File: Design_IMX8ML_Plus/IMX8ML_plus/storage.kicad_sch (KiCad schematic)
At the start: 3 parts, among them U1 MIMX8ML8CVNKZAB, U3 SDINBDG4-8G, U5 MT25QUxxxxxx1xW7

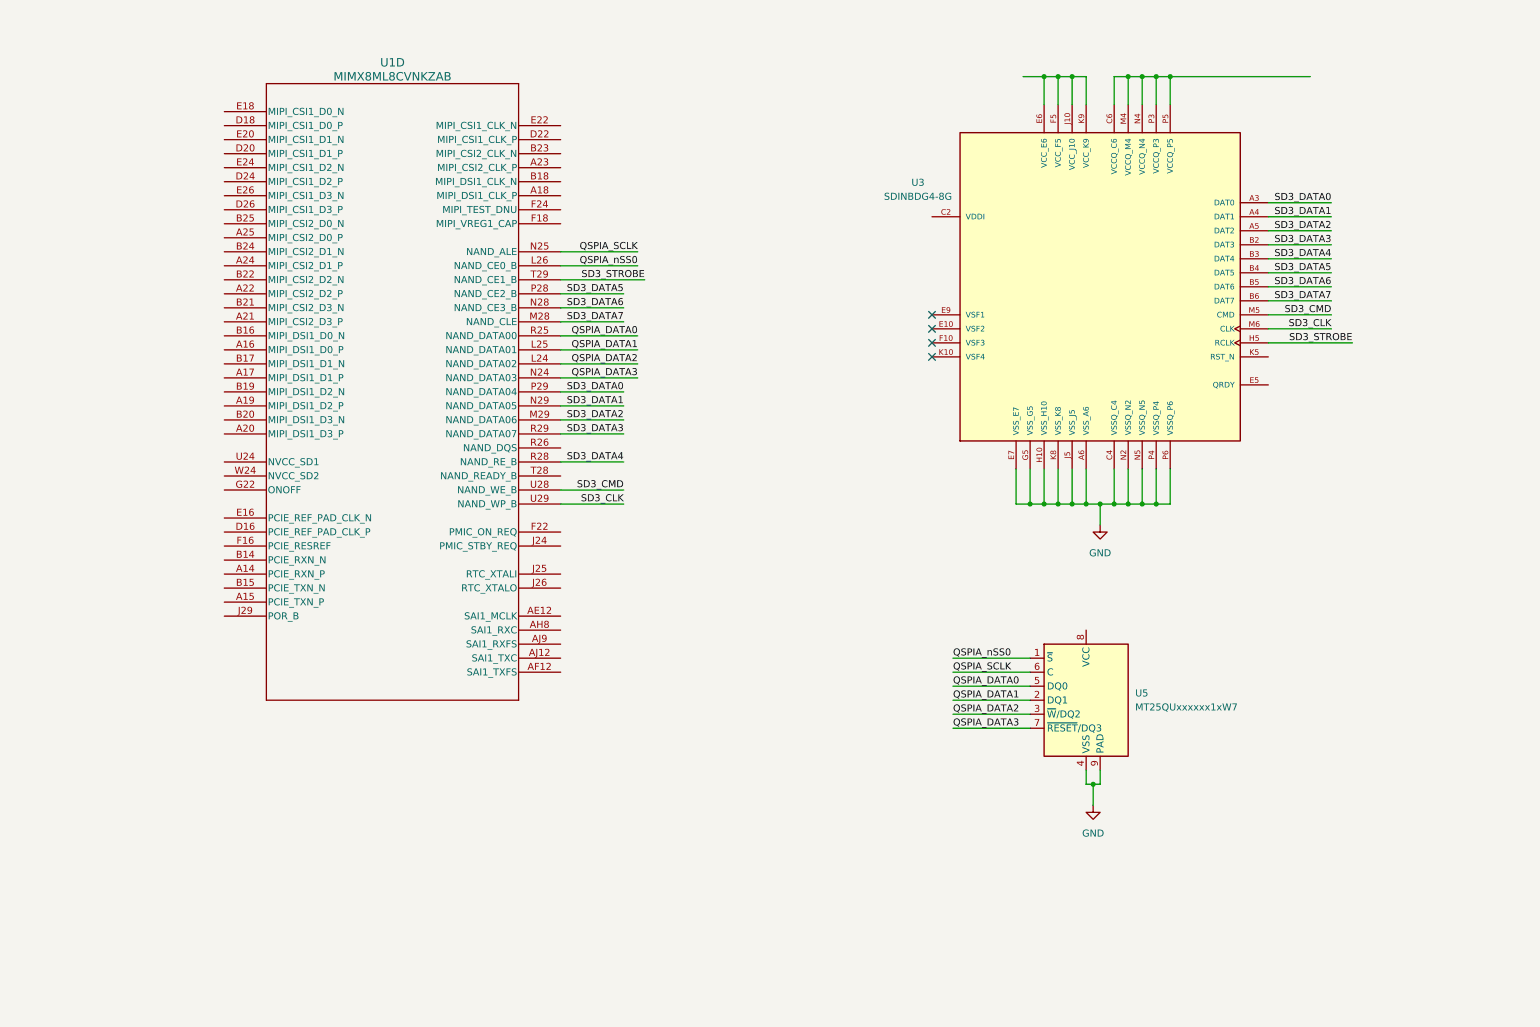
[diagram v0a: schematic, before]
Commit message: Add interface io pins
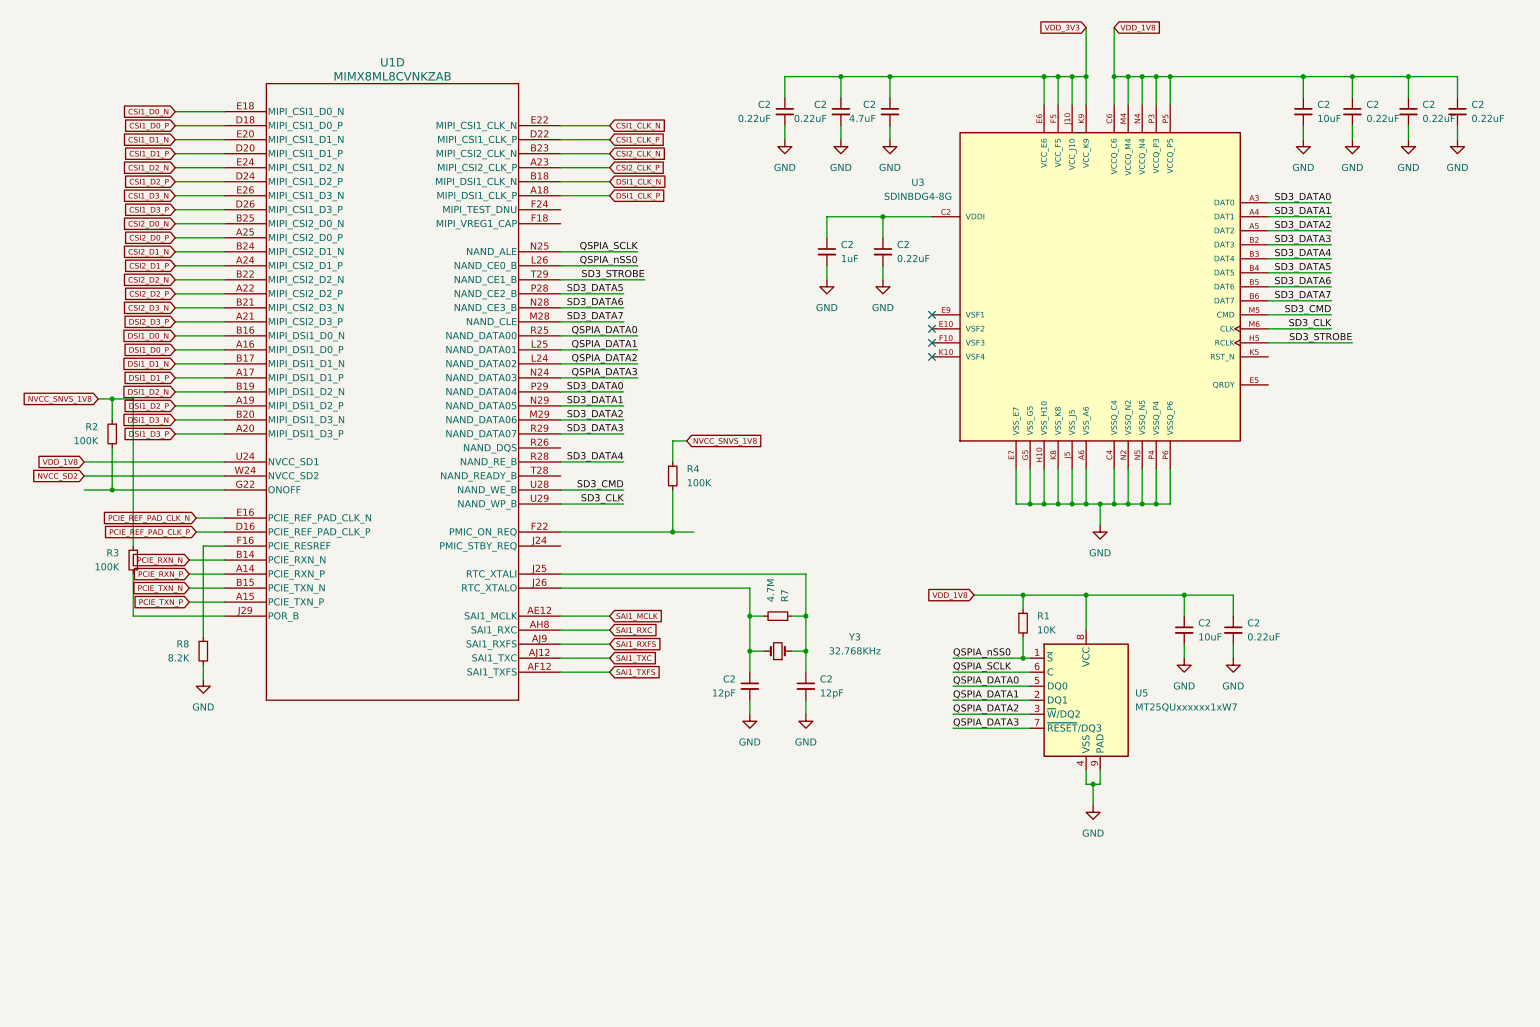
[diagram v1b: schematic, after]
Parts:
- added C2 (x7): 0.22uF, Capacitor_SMD:C_0201_0603Metric_Pad0.64x0.40mm_HandSolder, symbol Device:C_Small
- added C2: 4.7uF, Capacitor_SMD:C_0402_1005Metric_Pad0.74x0.62mm_HandSolder, symbol Device:C_Small
- added C2: 1uF, Capacitor_SMD:C_0201_0603Metric_Pad0.64x0.40mm_HandSolder, symbol Device:C_Small
- added C2 (x2): 12pF, Capacitor_SMD:C_0201_0603Metric_Pad0.64x0.40mm_HandSolder, symbol Device:C_Small
- added C2 (x2): 10uF, Capacitor_SMD:C_0402_1005Metric_Pad0.74x0.62mm_HandSolder, symbol Device:C_Small
- added R1: 10K, Resistor_SMD:R_0402_1005Metric_Pad0.72x0.64mm_HandSolder, symbol Device:R_Small
- added R2, R3, R4: 100K, Resistor_SMD:R_0402_1005Metric_Pad0.72x0.64mm_HandSolder, symbol Device:R_Small
- added R7: 4.7M, Resistor_SMD:R_0402_1005Metric_Pad0.72x0.64mm_HandSolder, symbol Device:R_Small
- added R8: 8.2K, Resistor_SMD:R_0402_1005Metric_Pad0.72x0.64mm_HandSolder, symbol Device:R_Small
- added Y3: 32.768KHz, Capacitor_SMD:C_0504_1310Metric, symbol Device:Crystal_Small
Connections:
- net GND: now also C2.2, C2.2, C2.2, C2.2, C2.2, C2.2, C2.2, C2.2, C2.2, C2.2, C2.2, C2.2, C2.2, R8.2
- net QSPIA_nSS0: now also R1.2
- net VDD_1V8: now reaches U5.8 (VCC)
- net VDD_1V8: now also U1.U24 (NVCC_SD1), U3.C6 (VCCQ_C6), U3.M4 (VCCQ_M4), U3.N4 (VCCQ_N4), U3.P3 (VCCQ_P3), U3.P5 (VCCQ_P5), C2.1, C2.1, C2.1, C2.1, C2.1, C2.1, R1.1
- net PCIE_RXN_P: now reaches U1.A14 (PCIE_RXN_P)
- net PCIE_TXN_P: now reaches U1.A15 (PCIE_TXN_P)
- net DSI1_D0_P: now reaches U1.A16 (MIPI_DSI1_D0_P)
- net DSI1_D1_P: now reaches U1.A17 (MIPI_DSI1_D1_P)
- net DSI1_CLK_P: now reaches U1.A18 (MIPI_DSI1_CLK_P)
- net DSI1_D2_P: now reaches U1.A19 (MIPI_DSI1_D2_P)
- net DSI1_D3_P: now reaches U1.A20 (MIPI_DSI1_D3_P)
- net DSI2_D3_P: now reaches U1.A21 (MIPI_CSI2_D3_P)
- net CSI2_D2_P: now reaches U1.A22 (MIPI_CSI2_D2_P)
- net CSI2_CLK_P: now reaches U1.A23 (MIPI_CSI2_CLK_P)
- net CSI2_D1_P: now reaches U1.A24 (MIPI_CSI2_D1_P)
- net CSI2_D0_P: now reaches U1.A25 (MIPI_CSI2_D0_P)
- net SAI1_MCLK: now reaches U1.AE12 (SAI1_MCLK)
- net SAi1_TXFS: now reaches U1.AF12 (SAI1_TXFS)
- net SAI1_RXC: now reaches U1.AH8 (SAI1_RXC)
- net SAI1_TXC: now reaches U1.AJ12 (SAI1_TXC)
- net SAI1_RXFS: now reaches U1.AJ9 (SAI1_RXFS)
- net PCIE_RXN_N: now reaches U1.B14 (PCIE_RXN_N)
- net PCIE_TXN_N: now reaches U1.B15 (PCIE_TXN_N)
- net DSI1_D0_N: now reaches U1.B16 (MIPI_DSI1_D0_N)
- net DSI1_D1_N: now reaches U1.B17 (MIPI_DSI1_D1_N)
- net DSI1_CLK_N: now reaches U1.B18 (MIPI_DSI1_CLK_N)
- net DSI1_D2_N: now reaches U1.B19 (MIPI_DSI1_D2_N)
- net DSI1_D3_N: now reaches U1.B20 (MIPI_DSI1_D3_N)
- net CSI2_D3_N: now reaches U1.B21 (MIPI_CSI2_D3_N)
- net CSI2_D2_N: now reaches U1.B22 (MIPI_CSI2_D2_N)
- net CSI2_CLK_N: now reaches U1.B23 (MIPI_CSI2_CLK_N)
- net CSI2_D1_N: now reaches U1.B24 (MIPI_CSI2_D1_N)
- net CSI2_D0_N: now reaches U1.B25 (MIPI_CSI2_D0_N)
- net PCIE_REF_PAD_CLK_P: now reaches U1.D16 (PCIE_REF_PAD_CLK_P)
- net CSI1_D0_P: now reaches U1.D18 (MIPI_CSI1_D0_P)
- net CSI1_D1_P: now reaches U1.D20 (MIPI_CSI1_D1_P)
- net CSI1_CLK_P: now reaches U1.D22 (MIPI_CSI1_CLK_P)
- net CSI1_D2_P: now reaches U1.D24 (MIPI_CSI1_D2_P)
- net CSI1_D3_P: now reaches U1.D26 (MIPI_CSI1_D3_P)
- net PCIE_REF_PAD_CLK_N: now reaches U1.E16 (PCIE_REF_PAD_CLK_N)
- net CSI1_D0_N: now reaches U1.E18 (MIPI_CSI1_D0_N)
- net CSI1_D1_N: now reaches U1.E20 (MIPI_CSI1_D1_N)
- net CSI1_CLK_N: now reaches U1.E22 (MIPI_CSI1_CLK_N)
- net CSI1_D2_N: now reaches U1.E24 (MIPI_CSI1_D2_N)
- net CSI1_D3_N: now reaches U1.E26 (MIPI_CSI1_D3_N)
- net at U1.F16 (PCIE_RESREF): now also R8.1
- net at U1.F22 (PMIC_ON_REQ): now also R4.2
- net at U1.G22 (ONOFF): now also R2.2
- net at U1.J25 (RTC_XTALI): now also C2.1, R7.1, Y3.1
- net at U1.J26 (RTC_XTALO): now also C2.1, R7.2, Y3.2
- net at U1.J29 (POR_B): now also R3.2
- net NVCC_SD2: now reaches U1.W24 (NVCC_SD2)
- net at U3.C2 (VDDI): now also C2.1, C2.1
- net VDD_3V3: now reaches U3.E6 (VCC_E6), U3.F5 (VCC_F5), U3.J10 (VCC_J10), U3.K9 (VCC_K9)
- net VDD_3V3: now also C2.1, C2.1, C2.1
- new net NVCC_SNVS_1V8: R2.1, R3.1, R4.1

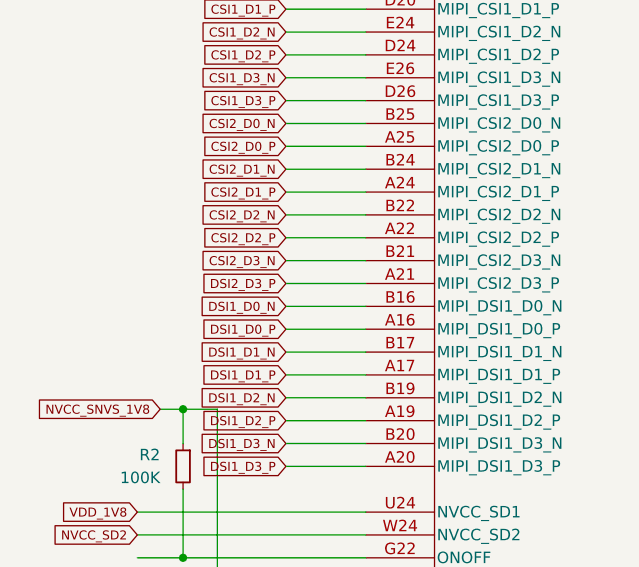
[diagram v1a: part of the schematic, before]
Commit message: Update schematic and add ethernet interface ksz9131rn
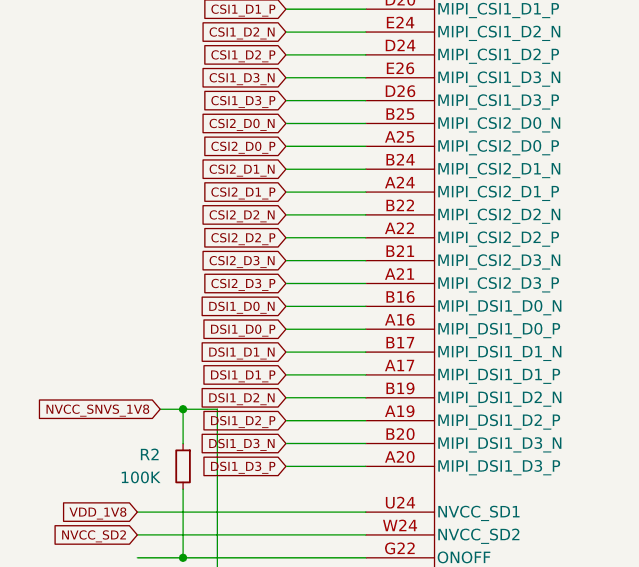
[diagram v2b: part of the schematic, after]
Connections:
- net DSI2_D3_P renamed CSI2_D3_P
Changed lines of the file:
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@@
     )
   )
-  (global_label "DSI2_D3_P" (shape input) (at 40.64 71.12 180) (fields_autoplaced)
+  (global_label "CSI2_D3_P" (shape input) (at 40.64 71.12 180) (fields_autoplaced)
     (effects (font (size 1 1)) (justify right))
     (property "Intersheetrefs" "${INTERSHEET_REFS}" (at 30.4949 71.12 0)

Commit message: Add SPB228 WIFI/BLE module
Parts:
- renumbered C2 to C144, C2 to C145, C2 to C85, C2 to C86, C2 to C87, C2 to C88, C2 to C89, C2 to C90, C2 to C91, C2 to C92, C2 to C93, C2 to C94, C2 to C95

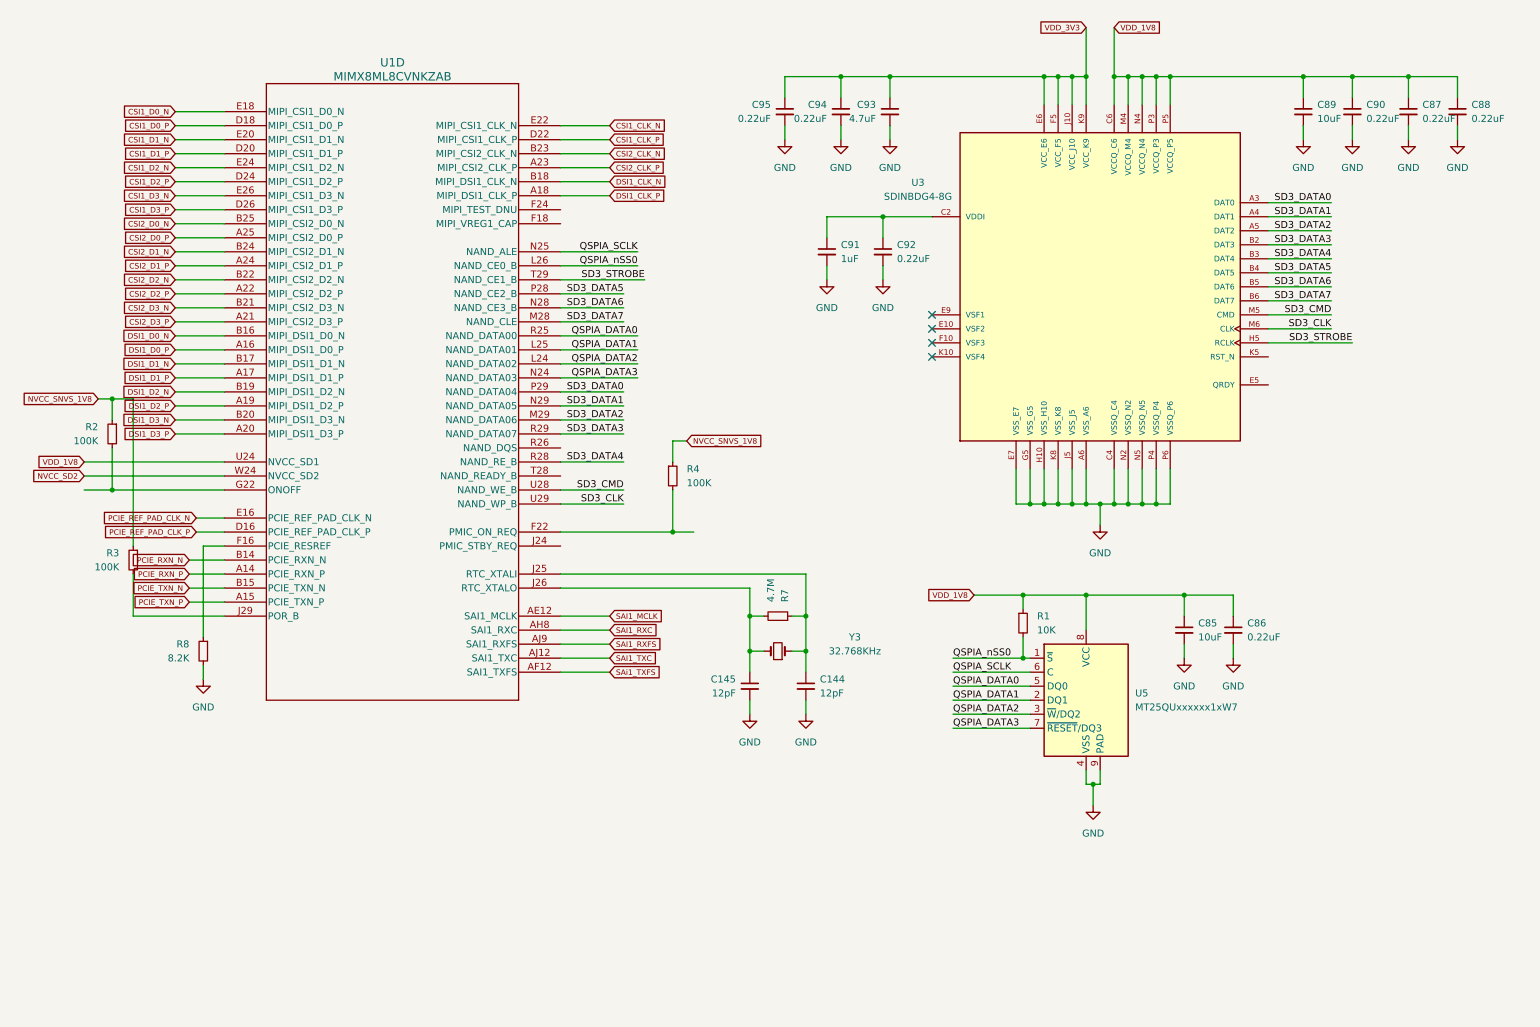
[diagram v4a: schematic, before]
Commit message: [IMX8ML-Processor] Reorganization of the pinout conector since processor to conectors
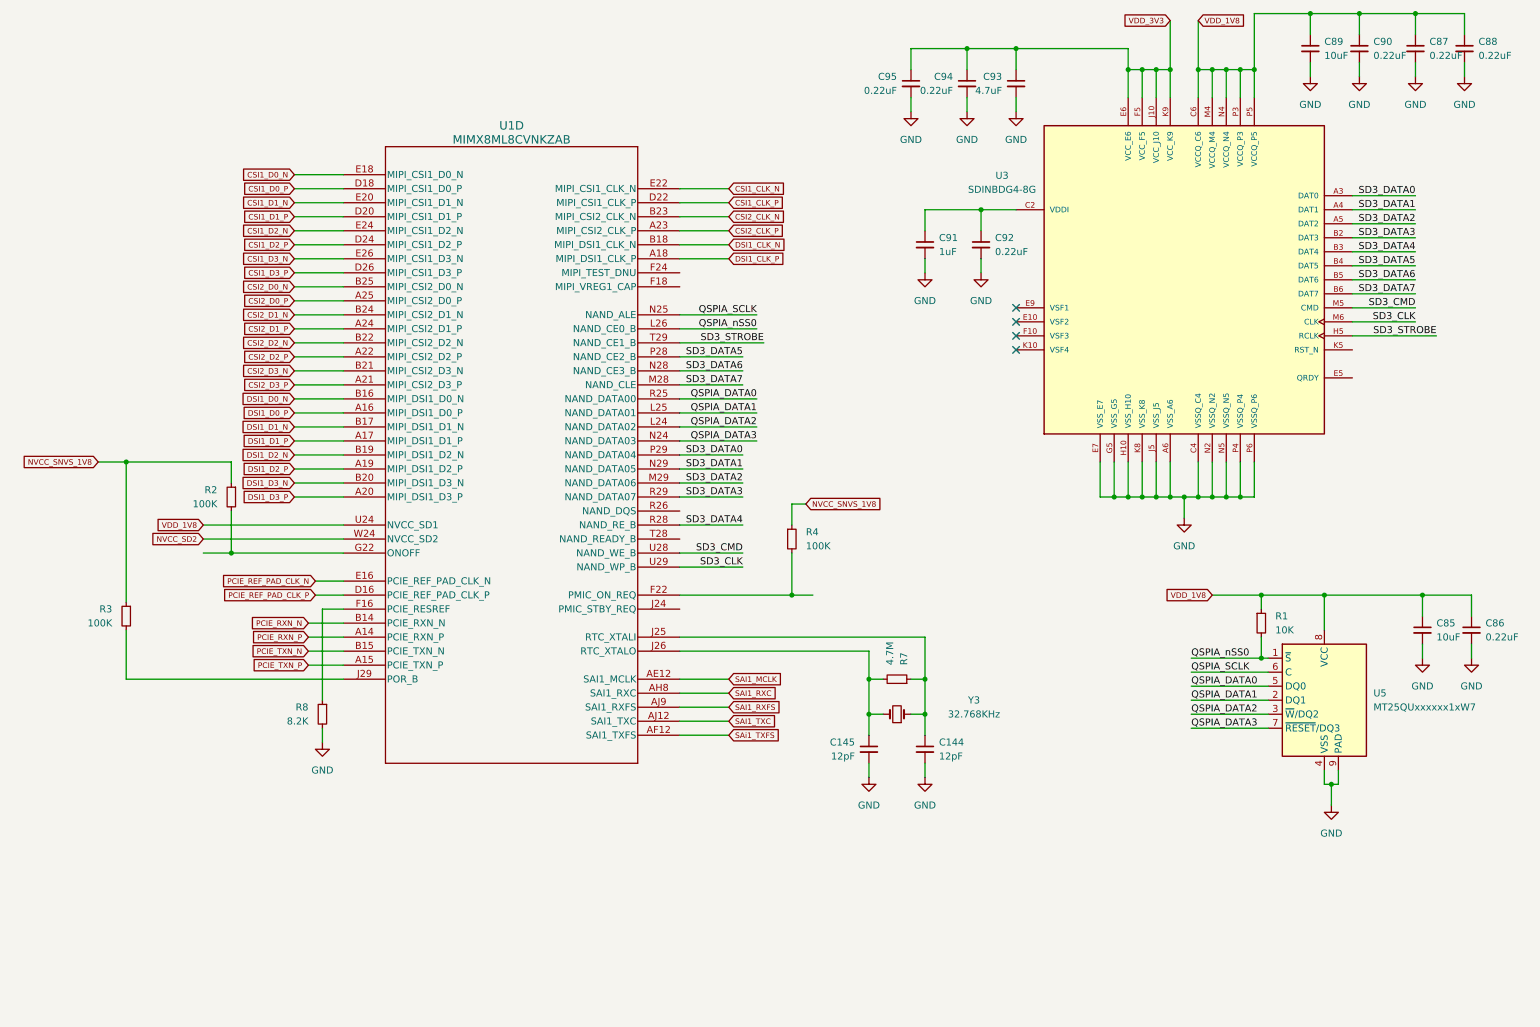
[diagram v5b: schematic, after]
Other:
- moved on the sheet: C144, C145, C85, C86, C87, C88, C89, C90, C91, C92, C93, C94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

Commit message: [PROCESSOR] Create zones It added power zones in the four layer
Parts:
- renumbered C145 to C115, C95 to C116, C91 to C117, C144 to C118, C94 to C119, C92 to C120, C93 to C121, C89 to C122, C90 to C123, C87 to C124, C85 to C125, C88 to C126, C86 to C127, R3 to R10, R2 to R11, R8 to R12, R4 to R13, R7 to R14, R1 to R15, U3 to U4, Y3 to Y2
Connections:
- net ON/OFF: now reaches R11.2, U1.G22 (ONOFF)
- net SAi1_TXFS renamed SAI1_TXFS
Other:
- note added: "ETH_2_RGMII_RXC"
- note added: "ETH_2_RGMII_RX_CTL"
- moved on the sheet: C115, C118, R10, R11, R14, Y2

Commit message: [BB_IMX8MLP IMX8MLP] Actuallizated to 9.0 kicad version
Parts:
- added R21: 100K, Resistor_SMD:R_0402_1005Metric, symbol Device:R_Small
- C115, C118: footprint Capacitor_SMD:C_0201_0603Metric_Pad0.64x0.40mm_HandSolder -> Capacitor_SMD:C_0201_0603Metric; MP (none) -> CGA1A2C0G1E120J030BA; Price (none) -> 0.1
- C116, C119, C120, C123, C124, C126, C127: footprint Capacitor_SMD:C_0201_0603Metric_Pad0.64x0.40mm_HandSolder -> Capacitor_SMD:C_0201_0603Metric; MP (none) -> LMK063BJ224MP-F; Price (none) -> 0.11
- C117: footprint Capacitor_SMD:C_0201_0603Metric_Pad0.64x0.40mm_HandSolder -> Capacitor_SMD:C_0201_0603Metric; MP (none) -> 02016D105MAT2A; Price (none) -> 0.1
- C121: footprint Capacitor_SMD:C_0402_1005Metric_Pad0.74x0.62mm_HandSolder -> Capacitor_SMD:C_0402_1005Metric; MP (none) -> C1005X5R0J475M050BC; Price (none) -> 0.4
- C122, C125: footprint Capacitor_SMD:C_0402_1005Metric_Pad0.74x0.62mm_HandSolder -> Capacitor_SMD:C_0402_1005Metric; MP (none) -> CL05A106MQ5NUNC; Price (none) -> 0.1
- R10, R11: footprint Resistor_SMD:R_0402_1005Metric_Pad0.72x0.64mm_HandSolder -> Resistor_SMD:R_0201_0603Metric; MP (none) -> RC0201FR-07100KL; Price (none) -> 0.1
- R12: footprint Resistor_SMD:R_0402_1005Metric_Pad0.72x0.64mm_HandSolder -> Resistor_SMD:R_0201_0603Metric; MP (none) -> RC0201FR-078K2L; Price (none) -> 0.1
- R13: footprint Resistor_SMD:R_0402_1005Metric_Pad0.72x0.64mm_HandSolder -> Resistor_SMD:R_0402_1005Metric
- R14: footprint Resistor_SMD:R_0402_1005Metric_Pad0.72x0.64mm_HandSolder -> Resistor_SMD:R_0402_1005Metric; MP (none) -> RC0201JR-074M3L (0201); Price (none) -> 0.1
- R15: footprint Resistor_SMD:R_0402_1005Metric_Pad0.72x0.64mm_HandSolder -> Resistor_SMD:R_0402_1005Metric; MP (none) -> CRCW040210K0JNED; Price (none) -> 0.1
- U1: footprint LFBGA548_SOT2047-1_NXP -> _W_SBC:LFBGA548_SOT2047-1_NXP; MP (none) -> -
- U4: footprint BGA153C50P14X14_1300X1150X80N -> _W_SBC:BGA153C50P14X14_1300X1150X80N; MP (none) -> -
- U5: MP (none) -> MT25QU256ABA1EW7-0SIT; Price (none) -> 4.5
- Y2: MP (none) -> ABS07-32.768KHZ-7-T; Price (none) -> 1
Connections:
- net GND: now also R10.2
- net NVCC_SNVS_1V8: now also R21.1; no longer R10.1
- net PMIC_ON_REQ: now reaches R13.2, U1.F22 (PMIC_ON_REQ)
- net PMIC_RST_B: now reaches U1.J24 (PMIC_STBY_REQ)
- net PMIC_RST_B: now also R10.1
- net POR_B: now reaches U1.J29 (POR_B)
- net POR_B: now also R21.2; no longer R10.2
